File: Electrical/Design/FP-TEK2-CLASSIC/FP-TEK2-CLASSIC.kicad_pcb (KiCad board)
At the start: 2 copper layers, 105.6 x 105.6 mm, 30 parts

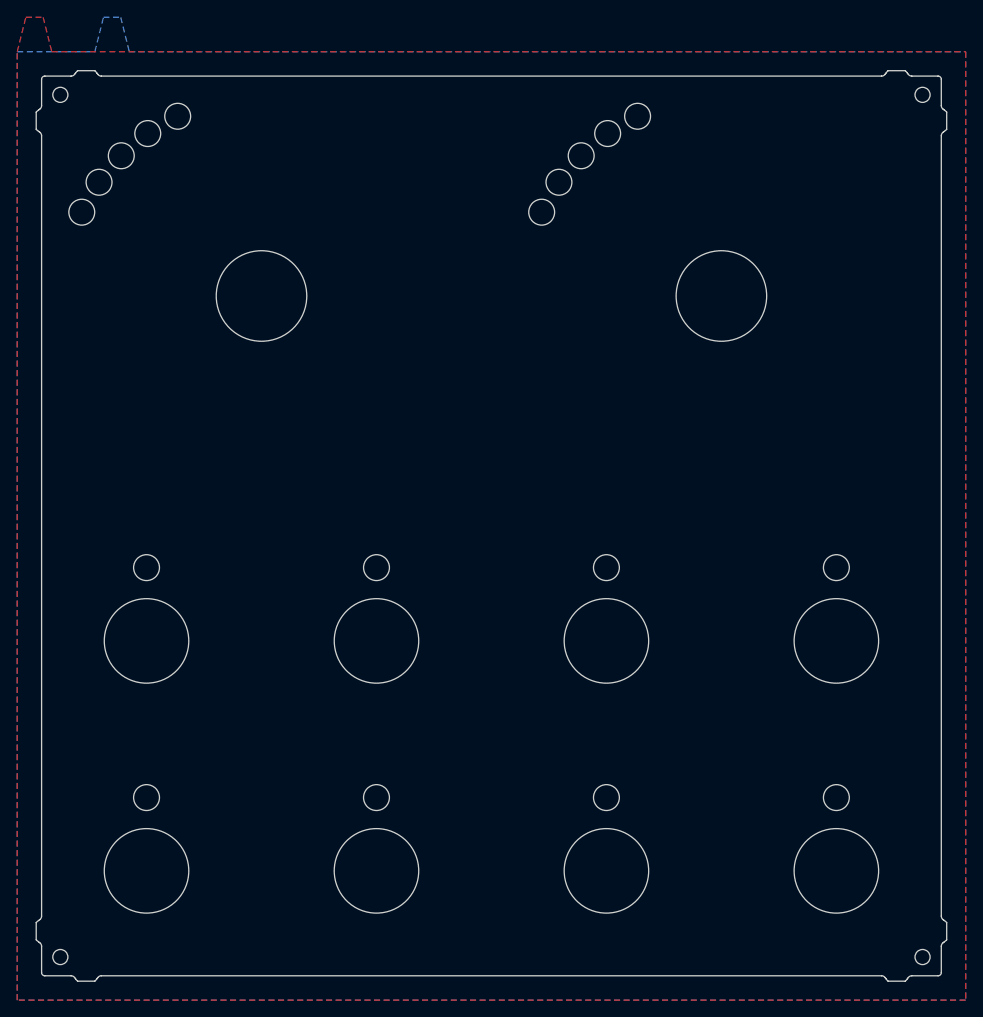
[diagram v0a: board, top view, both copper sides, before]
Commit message: SUKU rest of the frontpanels updated to use the plated through-hole for lightpipe
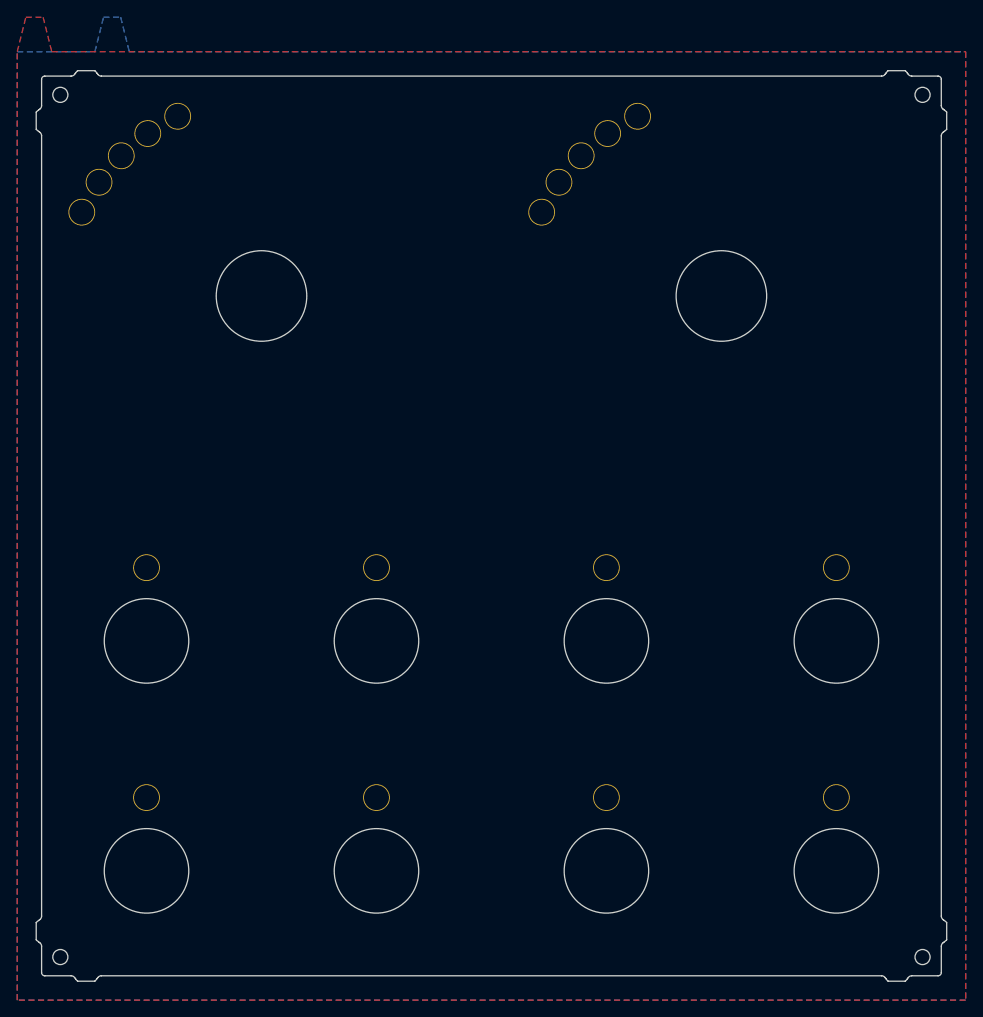
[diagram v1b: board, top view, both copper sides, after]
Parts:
- H501, H513, H514, H515, H516, H517, H518, H519, H520, H521, H523, H524, H525, H526, H527, H528, H529, H530: footprint suku_basics:FP_LED -> suku_basics:FP_LED_TIGHT
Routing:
- added copper zone on B.Cu, net GND
- added copper zone on F.Cu, net GND
- removed copper zone on B.Cu, net (none)
- removed copper zone on F.Cu, net (none)

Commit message: outline change + VSN window size change
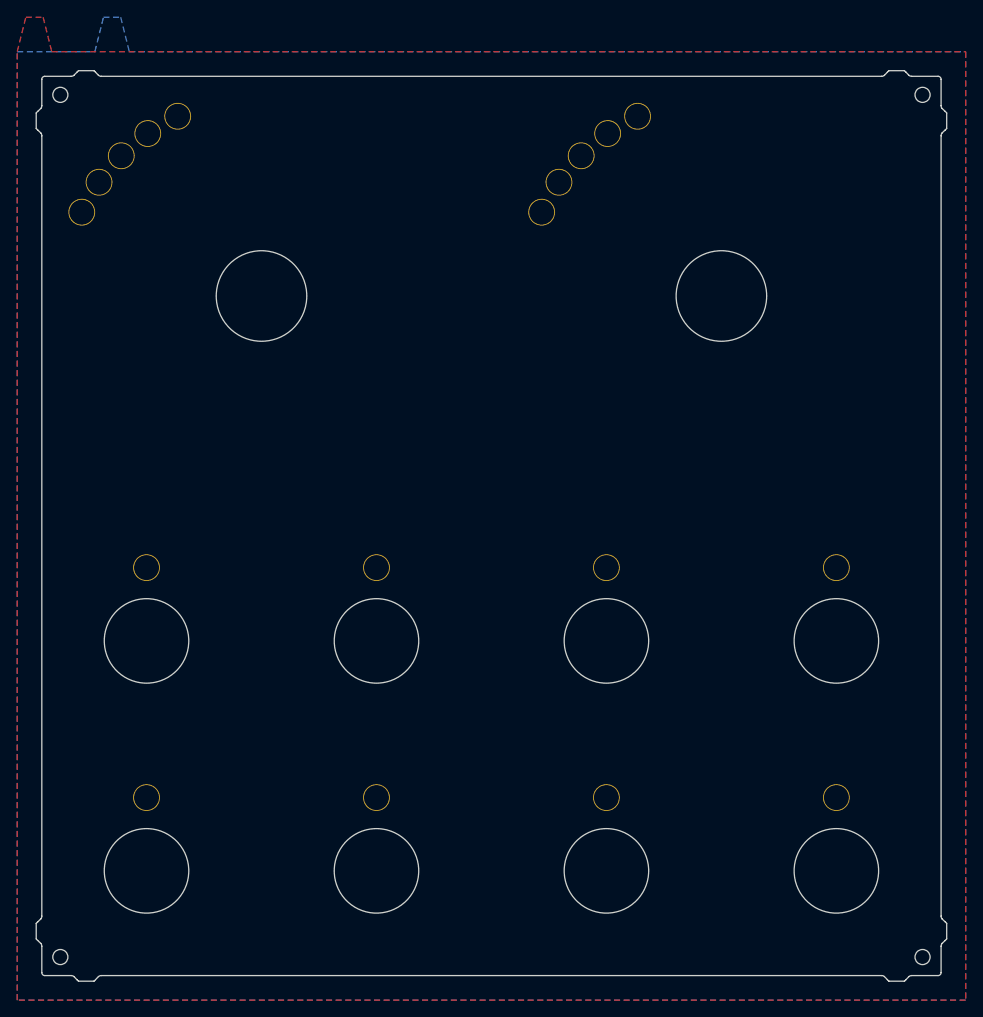
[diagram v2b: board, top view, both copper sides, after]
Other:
- outline, holes or cut-outs redrawn
